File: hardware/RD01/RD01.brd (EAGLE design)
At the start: 50 x 50 mm, 20 parts, among them J1 CON_TERMINAL_BLOCK_02-5MM, J2 CON_TERMINAL_BLOCK_02-5MM, J3 CON_TERMINAL_BLOCK_02-5MM, J4 CON_TERMINAL_BLOCK_02-5MM, K1 JS-M1-12V-5, K2 JS-M1-12V-5, Q1 BC337, Q2 BC337

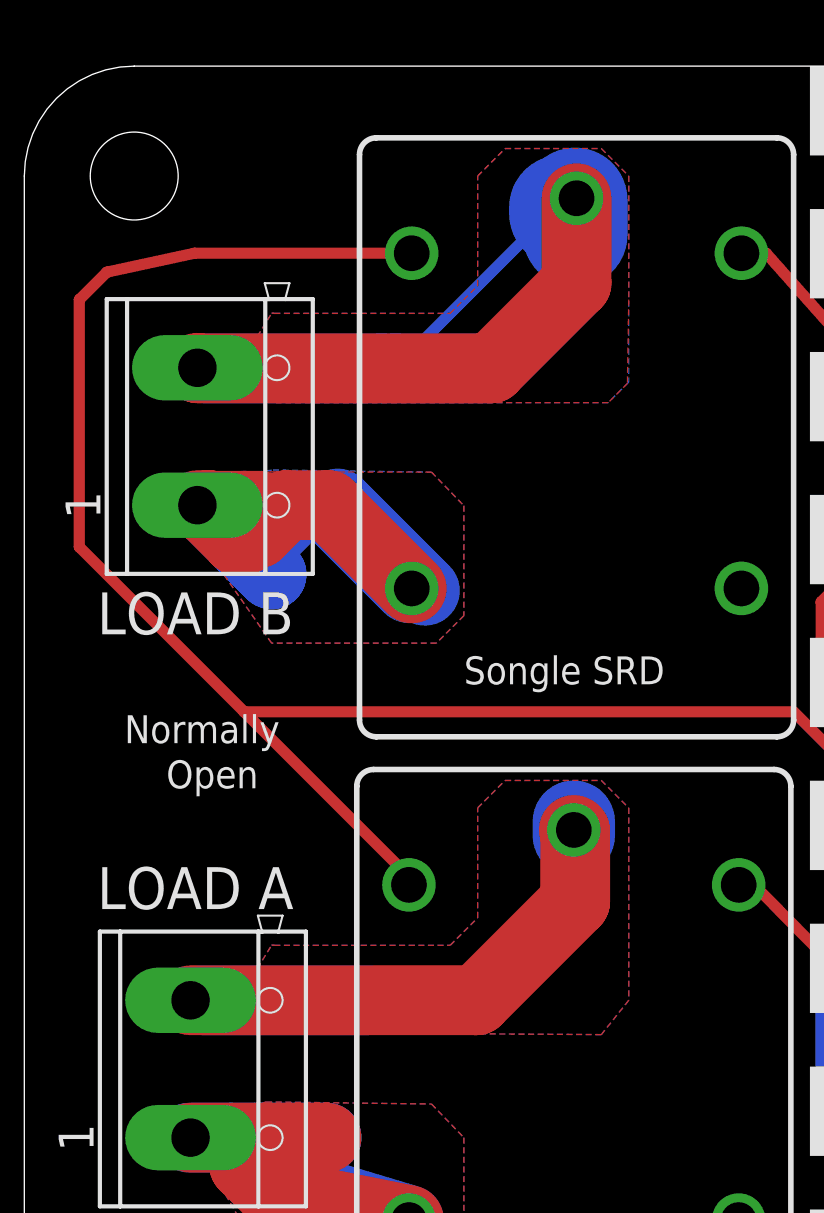
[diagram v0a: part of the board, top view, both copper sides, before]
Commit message: 2mm clearance
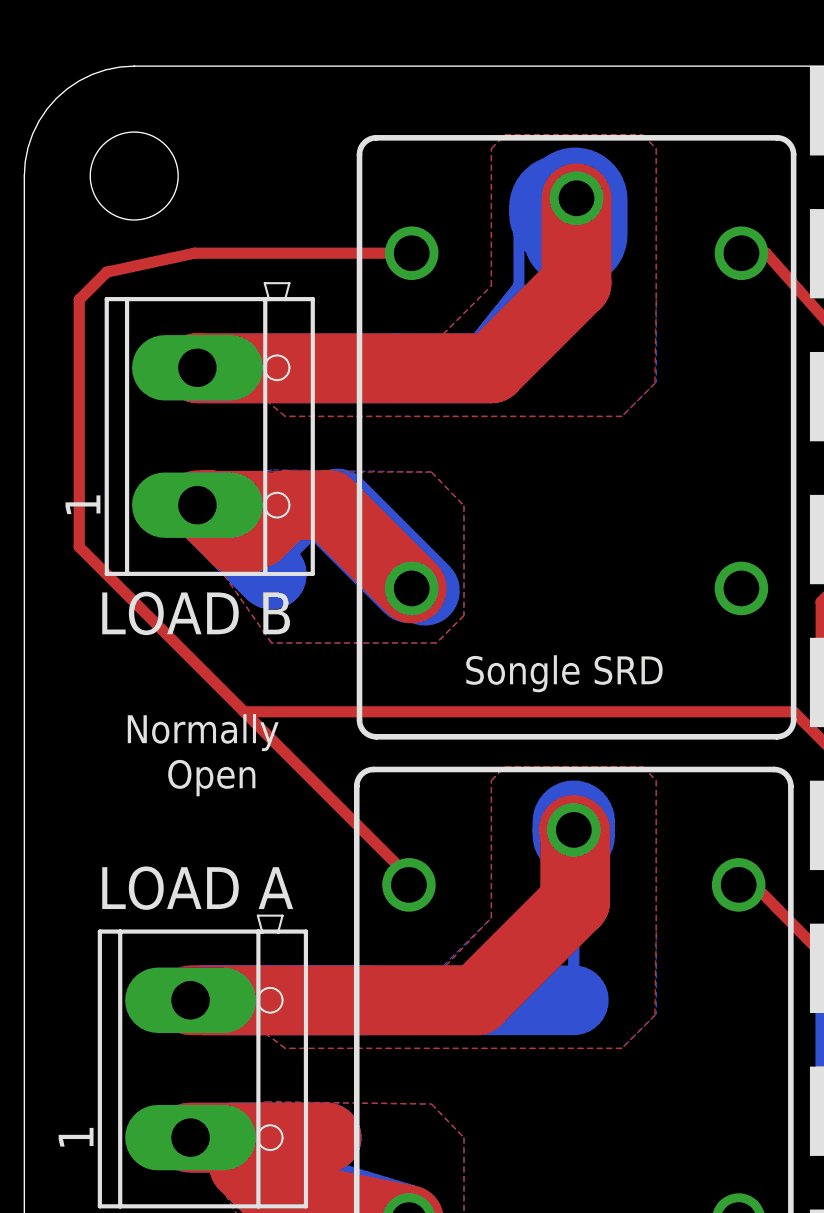
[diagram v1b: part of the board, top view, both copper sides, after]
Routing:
- net LOAD_A2: track 24.6 -> 44.3 mm
- net LOAD_B2: track 39.9 -> 41.6 mm
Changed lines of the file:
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@@
 <polygon width="0.254" layer="16">
 <vertex x="7.746" y="38.97"/>
-<vertex x="9" y="41" curve="-60"/>
-<vertex x="9.1" y="41"/>
-<vertex x="15.5" y="41"/>
-<vertex x="16.5" y="42"/>
-<vertex x="16.5" y="46"/>
-<vertex x="17.5" y="47"/>
-<vertex x="21" y="47"/>
-<vertex x="22" y="46"/>
-<vertex x="22" y="38.5"/>
-<vertex x="21.25" y="37.75"/>
-<vertex x="9" y="37.75"/>
-<vertex x="8.5" y="38"/>
+<vertex x="14.5" y="39.5" curve="-60"/>
+<vertex x="14.5" y="39.5"/>
+<vertex x="17" y="42"/>
+<vertex x="17" y="47"/>
+<vertex x="17.5" y="47.5"/>
+<vertex x="22.5" y="47.5"/>
+<vertex x="23" y="47"/>
+<vertex x="23" y="38.5"/>
+<vertex x="21.75" y="37.25"/>
+<vertex x="9.5" y="37.25"/>
+<vertex x="8" y="38.5"/>
 </polygon>
 <polygon width="0.254" layer="1">
 <vertex x="7.746" y="38.97"/>
-<vertex x="9" y="41" curve="-60"/>
-<vertex x="9.1" y="41"/>
-<vertex x="15.5" y="41"/>
-<vertex x="16.5" y="42"/>
-<vertex x="16.5" y="46"/>
-<vertex x="17.5" y="47"/>
-<vertex x="21" y="47"/>
-<vertex x="22" y="46"/>
-<vertex x="22" y="41.5"/>
-<vertex x="21.95" y="38.45"/>
-<vertex x="21.25" y="37.75"/>
-<vertex x="9" y="37.75"/>
-<vertex x="9" y="38"/>
-<vertex x="8.755" y="37.827"/>
-</polygon>
-<wire x1="6.5" y1="39" x2="13" y2="39" width="2.54" layer="16"/>
-<wire x1="13" y1="39" x2="13.5" y2="39" width="2.54" layer="16"/>
+<vertex x="14" y="39.5" curve="-60"/>
+<vertex x="14.1" y="39.5"/>
+<vertex x="14.5" y="39.5"/>
+<vertex x="17" y="42"/>
+<vertex x="17" y="47"/>
+<vertex x="17.5" y="47.5"/>
+<vertex x="22.5" y="47.5"/>
+<vertex x="23" y="47"/>
+<vertex x="23" y="41.5"/>
+<vertex x="22.95" y="38.45"/>
+<vertex x="21.75" y="37.25"/>
+<vertex x="9.5" y="37.25"/>
+<vertex x="8" y="38.5"/>
+</polygon>
+<wire x1="6.5" y1="39" x2="13.5" y2="39" width="2.54" layer="16"/>
 <wire x1="13.5" y1="39" x2="17" y2="39" width="2.54" layer="16"/>
 <wire x1="19.55" y1="44.63" x2="19.55" y2="44.86" width="3.81" layer="16"/>
-<wire x1="19.55" y1="44.86" x2="19.36" y2="44.86" width="0.4064" layer="16"/>
-<wire x1="19.36" y1="44.86" x2="13.5" y2="39" width="0.4064" layer="16"/>
+<wire x1="19.55" y1="44.86" x2="18" y2="44.86" width="0.4064" layer="16"/>
+<wire x1="18" y1="44.86" x2="18" y2="42" width="0.4064" layer="16"/>
+<wire x1="18" y1="42" x2="16" y2="39.5" width="0.4064" layer="16"/>
+<wire x1="16" y1="39.5" x2="13.5" y2="39" width="0.4064" layer="16"/>
 <wire x1="13.5" y1="39" x2="13" y2="38.5" width="0.4064" layer="16"/>
 </signal>
@@
 <wire x1="20.05" y1="19.59" x2="20.05" y2="22.15" width="2.54" layer="1"/>
 <wire x1="20.05" y1="22.15" x2="20" y2="22.2" width="2.54" layer="1"/>
+<wire x1="6.5" y1="16" x2="12.5" y2="16" width="2.54" layer="16"/>
+<wire x1="20" y1="22.5" x2="20" y2="22.2" width="3" layer="16"/>
+<wire x1="20" y1="22.2" x2="20" y2="22" width="3" layer="16"/>
+<wire x1="6.5" y1="16" x2="20" y2="16" width="2.54" layer="16"/>
+<wire x1="20" y1="16" x2="20" y2="22.2" width="0.4064" layer="16"/>
 <polygon width="0.254" layer="1">
 <vertex x="7.746" y="15.97"/>
-<vertex x="9" y="18" curve="-60"/>
-<vertex x="9.1" y="18"/>
-<vertex x="15.5" y="18"/>
-<vertex x="16.5" y="19"/>
-<vertex x="16.5" y="23"/>
-<vertex x="17.5" y="24"/>
-<vertex x="21" y="24"/>
-<vertex x="22" y="23"/>
-<vertex x="22" y="16"/>
-<vertex x="21" y="14.75"/>
+<vertex x="15.1" y="17"/>
+<vertex x="17" y="19"/>
+<vertex x="17" y="24"/>
+<vertex x="17.5" y="24.5"/>
+<vertex x="22.5" y="24.5"/>
+<vertex x="23" y="24"/>
+<vertex x="23" y="18.5"/>
+<vertex x="22.95" y="15.45"/>
+<vertex x="21.75" y="14.25"/>
+<vertex x="9.5" y="14.25"/>
+<vertex x="8.5" y="15"/>
 <vertex x="8.755" y="14.827"/>
 </polygon>
 <polygon width="0.254" layer="16">
-<vertex x="7.746" y="15.97"/>
-<vertex x="9" y="18" curve="-60"/>
-<vertex x="9.1" y="18"/>
-<vertex x="15.5" y="18"/>
-<vertex x="16.5" y="19"/>
-<vertex x="16.5" y="23"/>
-<vertex x="17.5" y="24"/>
-<vertex x="21" y="24"/>
-<vertex x="22" y="23"/>
-<vertex x="22" y="16"/>
-<vertex x="21" y="14.75"/>
-<vertex x="8.755" y="14.827"/>
-</polygon>
-<wire x1="6.5" y1="16" x2="12.5" y2="16" width="2.54" layer="16"/>
-<wire x1="20" y1="22.5" x2="20" y2="22" width="3" layer="16"/>
+<vertex x="9.246" y="16.47"/>
+<vertex x="15" y="17"/>
+<vertex x="17" y="19"/>
+<vertex x="17" y="24"/>
+<vertex x="17.5" y="24.5"/>
+<vertex x="22.5" y="24.5"/>
+<vertex x="23" y="24"/>
+<vertex x="23" y="15.5"/>
+<vertex x="21.75" y="14.25"/>
+<vertex x="9.5" y="14.25"/>
+<vertex x="8.5" y="15"/>
+</polygon>
 </signal>
 <signal name="COIL_A">

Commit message: RD01 Elecrow order
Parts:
- J2, J4: value CON_TERMINAL_BLOCK_02-5MM -> CON_TERMINAL_BLOCK_03-5MM; device dp_devices:TERMINAL_BLOCK_2P_5 -> dp_devices:TERMINAL_BLOCK_3P_5
- LED1, LED2: device SparkFun:LED5MM -> dp_devices:LED-3MM
- moved LED2 17.6 mm to (38.0, 45.5), turned to 0 degrees
- moved D1 13.9 mm to (43.5, 13.5), turned to 0 degrees
- moved R2 13.3 mm to (43.5, 8.50), turned to 0 degrees
- moved R1 13.1 mm to (43.5, 11.0), turned to 0 degrees
- moved D2 12.5 mm to (43.5, 41.5), turned to 0 degrees
- moved R6 10.6 mm to (43.5, 39.0), turned to 0 degrees
- moved Q1 9.78 mm to (36.8, 21.2)
- moved R3 9.60 mm to (43.5, 36.5), turned to 0 degrees
- moved R5 7.96 mm to (36.5, 37.8), turned to 90 degrees
- moved R4 6.39 mm to (36.5, 12.2)
- moved Q2 5.80 mm to (36.8, 28.8)
- moved J4 3.22 mm to (4.75, 34.0)
- moved J2 3.05 mm to (4.75, 16.0)
- moved K1 2.50 mm to (20.0, 16.0), turned to 0 degrees
- moved K2 2.50 mm to (20.1, 34.0), turned to 0 degrees
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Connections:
- net LOAD_A2 renamed LOAD_A_C
- net LOAD_B2 renamed LOAD_B_C
- removed net LOAD_A1: J2.1, K1.NO
- removed net LOAD_B1: J4.1, K2.NO
- new net LOAD_A_NC: J2.1, K1.NC
- new net LOAD_A_NO: J2.3, K1.NO
- new net LOAD_B_NC: J4.1, K2.NC
- new net LOAD_B_NO: J4.3, K2.NO
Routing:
- net LOAD_B1: track 39.4 -> 0.00 mm
- net VCC: track 127.4 -> 92.3 mm
- net LOAD_A1: track 28.7 -> 0.00 mm
- net LOAD_B_NO: track 0.00 -> 21.1 mm, vias 0 -> 1
- net LOAD_A_NC: track 0.00 -> 21.0 mm, vias 0 -> 1
- net LOAD_B_NC: track 0.00 -> 20.1 mm, vias 0 -> 1
- net LOAD_A_NO: track 0.00 -> 20.0 mm, vias 0 -> 1
- net N$6: track 4.79 -> 22.2 mm
- net GND: track 55.9 -> 39.5 mm
- net RELAY_B: track 23.5 -> 10.8 mm
- net COIL_B: track 14.1 -> 23.5 mm
- net RELAY_A: track 9.29 -> 18.2 mm
- net COIL_A: track 14.0 -> 22.6 mm
- net N$1: track 4.78 -> 9.56 mm
- net LOAD_B_C: track 41.6 -> 43.5 mm, vias 0 -> 2
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- removed copper zone on layer 1, net LOAD_A1
- removed copper zone on layer 16, net LOAD_A1
- removed copper zone on layer 1, net LOAD_A_C
- removed copper zone on layer 16, net LOAD_A_C
- removed copper zone on layer 1, net LOAD_B1
- removed copper zone on layer 16, net LOAD_B1
- removed copper zone on layer 1, net LOAD_B_C
- removed copper zone on layer 16, net LOAD_B_C
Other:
- board text added: "C"
- board text added: "Magic Smoke"
- board text added: "NC"
- board text added: "NO"
- board text added: "RD01"
- board text removed: "10A 250VAC"
- board text removed: "LOAD A"
- board text removed: "LOAD B"
- board text removed: "Magic Smoke RB02"
- board text removed: "Magic Smoke RD01"
- board text removed: "Normally"
- board text removed: "Open"
